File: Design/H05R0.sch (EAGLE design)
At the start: 62 parts, among them J1 1984617_MOD, Q1 ECH8693R-TL-W, Q2 ECH8693R-TL-W, U1 STM32G0B1CEU6QFN_B1CEU6_STM-L, U2 MAX17330X22+, U3 TPS631000DRLR, U4 LD39200PU33R, U5 NCP45521IMNTWG-LDFN8_2X2_ONS, X1 XTALL_CSTCE8M00G52

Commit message: - New version: Schematic finished and reviewed. Other files have not been modified yet for the new design.
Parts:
- removed D2: UCLAMP0501H.TCT, HEXABITZ_RCLS:UCLAMP0501H.TCT
- removed J1: 1984617_MOD, HEXABITZ_CONNECTION_PARTS:1984617_MOD
- removed Q2: ECH8693R-TL-W, HEXABITZ_RCLS:ECH8693R-TL-W
- removed R1: 0.0R, HEXABITZ_RCLS:R-0603
- added BAT_J2: B2P-VH-FB-B_LF__SN_, HEXABITZ_CONNECTION_PARTS:B2P-VH-FB-B_LF__SN_
- added C19: 10uF, HEXABITZ_RCLS:C-0805
- added C20, C6: 1uF, HEXABITZ_RCLS:C-0805
- added C21, C22, C23: 100nF, HEXABITZ_RCLS:C-0603
- added C24: 22nF, HEXABITZ_RCLS:C-0603
- added C7: 4.7uF, HEXABITZ_RCLS:C-0805
- added PIO_J: 3-644456-2, HEXABITZ_USER_INTERFACE_PARTS:3-644456-2
- added R25, R28: 100K, HEXABITZ_RCLS:R-0603
- added R26, R27: 4.7K, HEXABITZ_RCLS:R-0603
- added R29: 100R, HEXABITZ_RCLS:R-0603
- added R30: 0R, HEXABITZ_RCLS:R-0603
- added SJ1, SJ2: (no value), jumper:SJ
- added U6: LDK130C33R, HEXABITZ_ICs:LDK130C33R
- added VBUS_OUT_J: 1984617, HEXABITZ_CONNECTION_PARTS:1984617
- Q1: value ECH8693R-TL-W -> SISF06DN-T1-GE3; device HEXABITZ_RCLS:ECH8693R-TL-W -> HEXABITZ_ICs:SISF06DN-T1-GE3
- R4: value 10 mR -> 5 mR
- R5: value 100K -> 33K
- R6: value 665K -> 220K
- U5: value NCP45521IMNTWG-LDFN8_2X2_ONS -> NCP45521IMNTWG-L
- USB_C: value UJC-HP-G-SMT-TR -> 12401610E4#2A; device HEXABITZ_CONNECTION_PARTS:UJC-HP-G-SMT-TR -> HEXABITZ_CONNECTION_PARTS:12401610E4#2A
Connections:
- net DIS renamed N$24
- removed net CHG: R9.2, U2.CHG
- removed net CSP: C18.1, Q1.SOURCE1, Q2.SOURCE1, R4.2, U2.CSP
- removed net N$13 (its old number): R20.2, R7.2, U3.MODE
- removed net N$4: Q2.DRAIN_1, Q2.DRAIN_2, Q2.DRAIN_3, Q2.DRAIN_4
- removed net N$9: Q1.DRAIN_1, Q1.DRAIN_2, Q1.DRAIN_3, Q1.DRAIN_4
- removed net VSSA: BAT_J.2, C10.1, C11.1, C13.2, C14.2, C17.1, C2.2, C3.-, C4.2, C5.-, C8.-, C9.1, D2.A, EXT_TH_J.1, J1.2, R1.1, R13.1, R14.1, R19.2, R5.1, R7.1, U1.VSS/VSSA, U2.GND, U3.GND, U4.EPAD, USB_C.GND, USB_C.SHIELD
- new net 3V3_OUT: C15.2, SJ2.1, U$1.VDD1, U$1.VDD10, U$1.VDD2, U$1.VDD3, U$1.VDD4, U$1.VDD5, U$1.VDD6, U$1.VDD7, U$1.VDD8, U$1.VDD9, U4.ADJ/SENSE, U4.OUT
- new net 3V3_OUT_EN: R28.2, U4.EN
- new net MCU_3V3: C21.2, C7.1, R11.2, R21.2, R22.2, SJ2.2, U5.VCC, U6.OUT
- new net N$16: R8.2, U3.EN
- new net N$22: R25.1, U6.EN
- new net N$23: R29.2, U5.BLEED
- new net N$25: Q1.G1, R9.1
- new net N$29: C23.2, U5.SR
- new net N$30: C18.1, Q1.S1, R4.2, U2.CSP
- new net N$32: C18.2, R9.2, U2.CHG
- new net VBUS_OUT: C20.1, R29.1, SJ1.2, U5.VOUT, VBUS_OUT_J.1
- new net VBUS_OUT_EN: U5.EN
- new net VBUS_SENSE: C22.1, R26.1, R27.2
- net +3.8V: now also C6.1, R25.2, U6.IN; no longer U4.EN
- net GND: now also BAT_J.2, BAT_J2.2, C10.1, C11.1, C13.2, C14.2, C17.1, C19.2, C2.2, C20.2, C21.1, C22.2, C23.1, C24.1, C3.-, C4.2, C5.-, C6.2, C7.2, C8.-, C9.1, EXT_TH_J.2, PIO_J.2, R13.1, R14.1, R19.2, R27.1, R28.1, R5.1, R7.1, U1.VSS/VSSA, U2.GND, U3.GND, U5.GND, U6.GND, USB_C.GND, USB_C.MH, VBUS_OUT_J.2; no longer R1.2
- net MCU_INT: now also PIO_J.1
- net MCU_SCL: no longer R21.1
- net MCU_SDA: now also R21.1
- net N$10: now also Q1.G2, R10.1; no longer C18.2, Q1.GATE1, Q2.GATE1, R9.1
- net N$15: now also Q1.D1, Q1.D2; no longer Q1.GATE2, Q2.GATE2, R10.1
- net N$18: now also EXT_TH_J.1, R30.1; no longer EXT_TH_J.2
- net N$28: now also R20.1, R7.2, U3.MODE; no longer R8.1, U3.EN
- net VBAT: now also BAT_J2.1, C24.2, R30.2
- net VBUS: now also C19.1, Q1.S2, R20.2, R26.2, R8.1, SJ1.1, U5.VIN; no longer D2.K, J1.1, Q1.SOURCE2, Q2.SOURCE2, R20.1, R8.2
- net VDD: no longer C15.2, R11.2, R21.2, R22.2, U$1.VDD1, U$1.VDD10, U$1.VDD2, U$1.VDD3, U$1.VDD4, U$1.VDD5, U$1.VDD6, U$1.VDD7, U$1.VDD8, U$1.VDD9, U4.ADJ/SENSE, U4.OUT
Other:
- note added: "3"
- note added: "3.3V Out LDO"
- note added: "Active High"
- note added: "Active Low"
- note added: "Charger input"
- note added: "MCU LDO"
- note added: "VBUS Output Switch"
- note removed: "BAT_I2C"
- note removed: "LDO Regulator"
- note removed: "Power input"

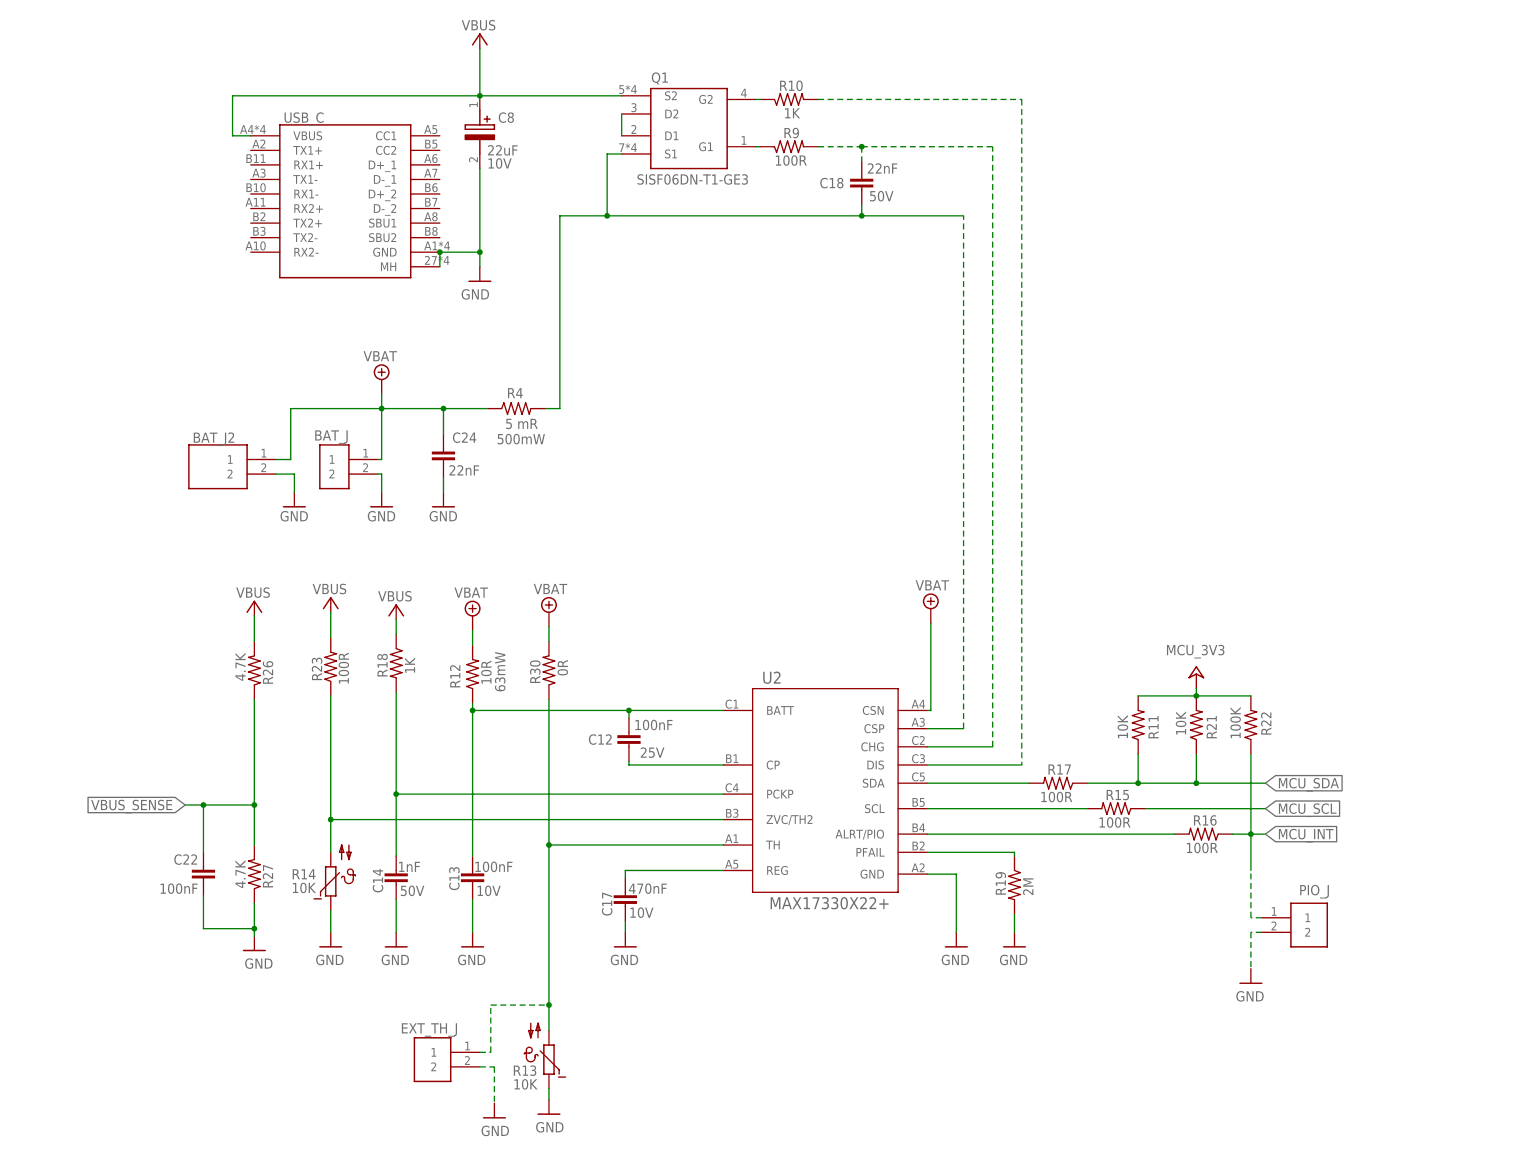
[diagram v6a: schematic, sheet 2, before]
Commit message: -New Version (1b), reviewed and finished - adding the charging detection & current measurement circuit
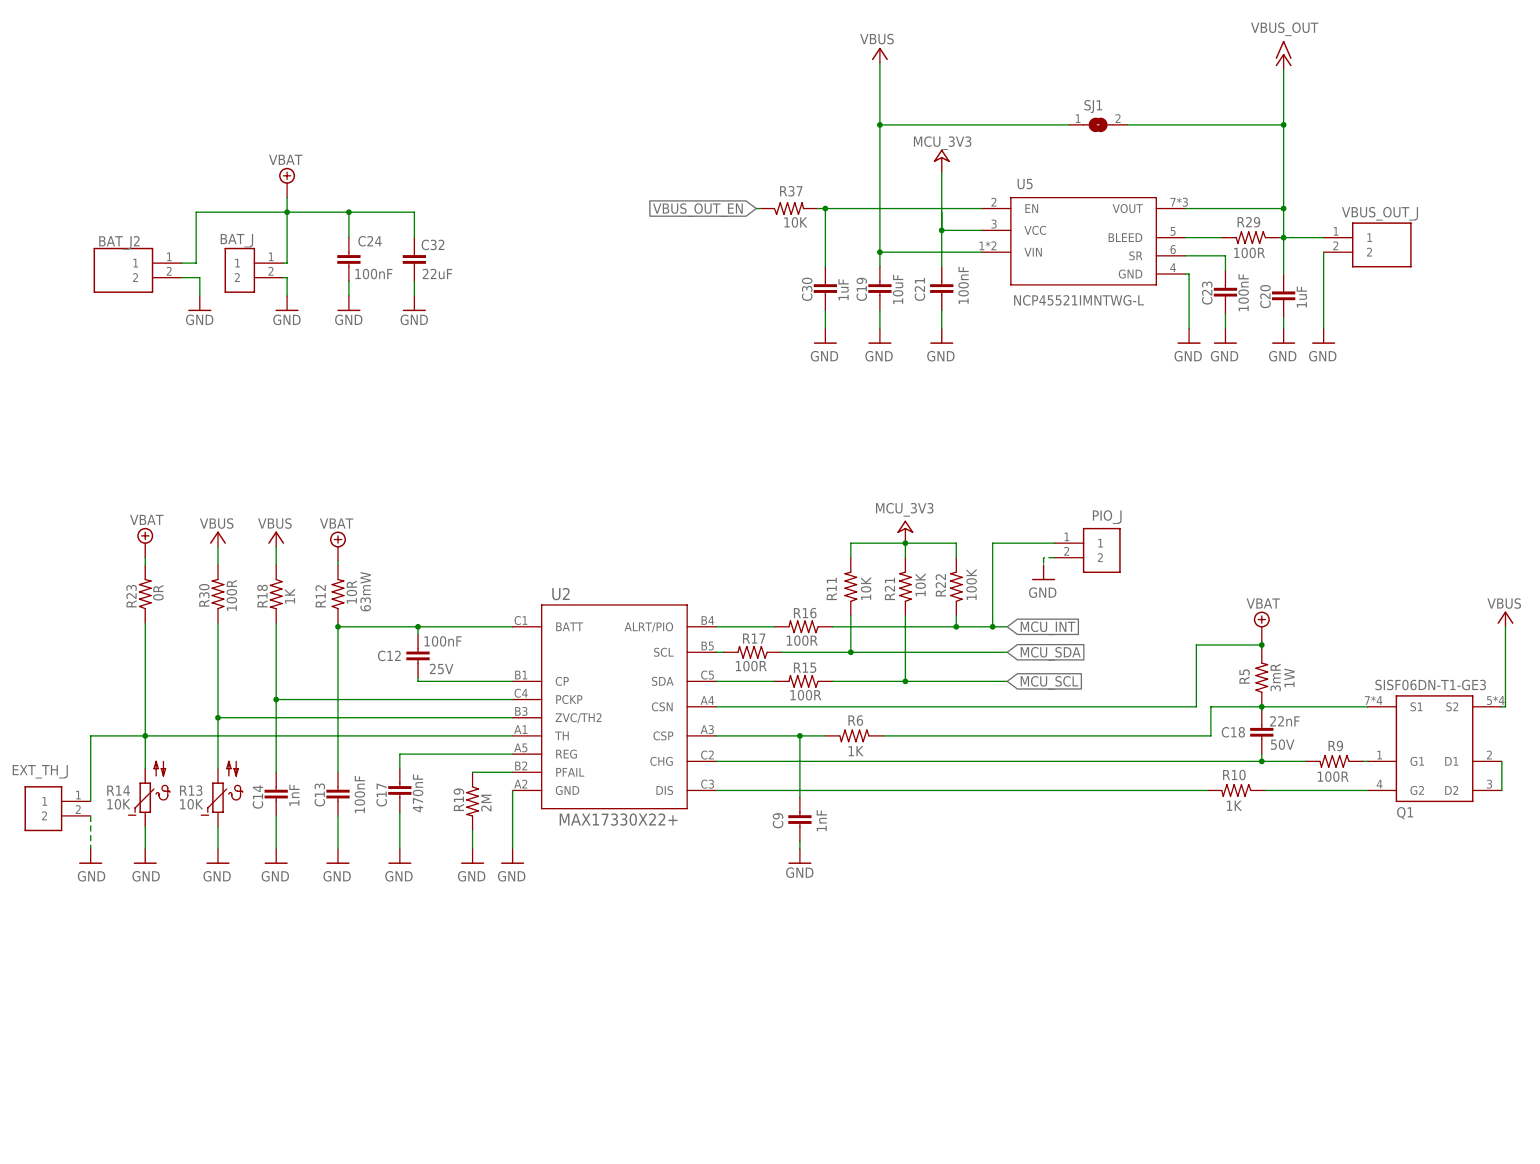
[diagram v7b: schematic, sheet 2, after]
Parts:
- removed L1: DFE252012P-1R0M=P2, HEXABITZ_RCLS:DFE252012P-1R0M=P2
- removed USB_C: 12401610E4#2A, HEXABITZ_CONNECTION_PARTS:12401610E4#2A
- added C25, C26, C27, C31: 100nF, HEXABITZ_RCLS:C-0603
- added C28, C29, C30: 1uF, HEXABITZ_RCLS:C-0805
- added C32: 22uF, HEXABITZ_RCLS:C-0805
- added D2: TL431QDBZR,215, HEXABITZ_RCLS:TL431QDBZR,215
- added D5, D6, D7: CUS10S30,H3F, HEXABITZ_RCLS:CUS10S30,H3F
- added J1: 12401610E4#2A12401610E42A, HEXABITZ_CONNECTION_PARTS:12401610E4#2A12401610E42A
- added R1: 10 mR, HEXABITZ_RCLS:R-0805
- added R31: 20K, HEXABITZ_RCLS:R-0603
- added R32: 27K, HEXABITZ_RCLS:R-0603
- added R33: 2K, HEXABITZ_RCLS:R-0603
- added R34: 100K, HEXABITZ_RCLS:R-0603
- added R35, R36: 22K, HEXABITZ_RCLS:R-0603
- added R37, R39: 10K, HEXABITZ_RCLS:R-0603
- added R38: 1M, HEXABITZ_RCLS:R-0603
- added SJ3: (no value), HEXABITZ_USER_INTERFACE_PARTS:SJ
- C10: value 47uF -> 33nF; MPN CL10A476MQ8QRN -> (none); VOLTAGE_RATING 6.3V -> 50V
- C11, C15: device HEXABITZ_RCLS:C-0603 -> HEXABITZ_RCLS:C-0805
- C16: value 22pF -> 33nF; STATE DNP -> (none); VOLTAGE_RATING (none) -> 50V
- C24: value 22nF -> 100nF
- C8: device HEXABITZ_RCLS:T491B226K010AT -> HEXABITZ_RCLS:C-0805; VOLTAGE 10V -> (none)
- C9: value 22uF -> 1nF; MPN GRM187R61A226ME15 -> (none); VOLTAGE_RATING 10V -> 50V
- R20: value 100K -> 49.9K
- R23: RESISTANCE 100R -> 0R
- R25, R28: value 100K -> 220K
- R26: value 4.7K -> 47K
- R27: value 4.7K -> 20K
- R30: value 0R -> 100R
- R4: value 5 mR -> 1K; device HEXABITZ_RCLS:R-0805 -> HEXABITZ_RCLS:R-0603; POWR 500mW -> (none); STATE (none) -> DNP
- R5: value 33K -> 3mR; device HEXABITZ_RCLS:R-0603 -> HEXABITZ_RCLS:R_1206R1206; MPN (none) -> WFC12063L000FE66; OCTOPART_URL (none) -> https://www.digikey.com/en/products/detail/vishay-dale/WFC1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; POWER (none) -> 1W; TOLERANCE 1% -> (none)
- R6: value 220K -> 1K; TOLERANCE 1% -> (none)
- R7: value 100K -> 1K; STATE (none) -> DNP
- R8: value 100K -> 49.9K; STATE (none) -> DNP
- SJ1, SJ2: device jumper:SJ -> HEXABITZ_USER_INTERFACE_PARTS:SJ
- U3: value TPS631000DRLR -> TSV772IQ2T; device HEXABITZ_ICs:TPS631000DRLRTPS631000DRLR_TEX -> HEXABITZ_ICs:TSV772IQ2T
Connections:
- net BAT_ALRT renamed N$15
- net N$2 renamed IND_LED
- removed net +3.8V: C10.2, C11.2, C16.1, C6.1, R25.2, R6.1, U3.VOUT, U4.IN, U6.IN
- removed net BAT_SCL: R15.2, U2.SCL
- removed net BAT_SDA: R17.2, U2.SDA
- removed net N$13 (its old number): L1.1, U3.LX1
- removed net N$18 (its old number): EXT_TH_J.1, R13.2, R30.1, U2.TH
- removed net USART5_RX: U$1.SD1, U1.PD2
- removed net USART5_TX: U$1.SU1, U1.PD3
- removed net VDD: D4.C, FB1.2
- new net 3V3_OUT_PG: R39.1, U1.PB13, U4.PG
- new net CHARGER_CURRENT_SENSE: C10.2, R20.2, U1.PB0, U3.OUT1
- new net CHARGER_DETECT: D5.A, R38.2, U3.OUT2
- new net MCU_LDO_EN: D6.A, U1.PB2
- new net N$11: C9.2, R6.2, U2.CSP
- new net N$12: C18.1, Q1.S1, R5.1, R6.1
- new net N$24: R15.2, U2.SDA
- new net N$32: D5.K, D6.K, D7.K, R35.1
- new net N$35: D7.A, SJ3.1
- new net N$4: C30.2, R37.2, U5.EN
- new net USART4_RX: U$1.SD1, U1.PA1
- new net USART4_TX: U$1.SU1, U1.PA0
- new net VBUS1: C26.2, R31.1, R32.2, R38.1, U3.IN2+
- new net VBUS2: C27.2, D2.1, D2.2, R33.1, R34.2, U3.IN2-
- new net VCHARGER: C25.2, C31.2, C8.1, J1.VBUS, R1.1, R7.2, U3.VCC+
- new net VREF: C4.1, C5.+, U1.VREF+
- net 3V3_OUT: now also U4.SENSE; no longer U4.ADJ/SENSE
- net 3V3_OUT_EN: now also R36.1, U1.PB12; no longer R28.2, U4.EN
- net GND: now also C16.1, C25.1, C26.1, C27.1, C28.1, C29.1, C30.1, C31.1, C32.2, C8.2, D2.3, J1.GND, J1.MH, R25.2, R32.1, R34.1, R8.1, U3.VCC-; no longer C10.1, C8.-, R5.1, R7.1, U1.PB12, U1.PB13, U3.GND, USB_C.GND, USB_C.MH
- net MCU_3V3: now also D4.C, FB1.2, R39.2
- net MCU_INT: now also U1.PA5; no longer U1.PB0
- net MCU_SCL: now also R21.1
- net MCU_SDA: no longer R21.1
- net N$14: now also C10.1, R20.1, R4.1, U3.IN1-; no longer L1.2, U3.LX2
- net N$16: now also R17.2, U2.SCL; no longer R8.2, U3.EN
- net N$17: now also R13.2, R30.1; no longer R14.2, R23.1
- net N$22: now also C28.2, R35.2
- net N$27: now also R7.1, R8.2, U3.IN1+; no longer R5.2, R6.2, U3.FB
- net N$28: now also EXT_TH_J.1, R14.2, R23.1, U2.TH; no longer R20.1, R7.2, U3.MODE
- net N$30: now also C29.2, R28.2, R36.2, U4.EN; no longer C18.1, Q1.S1, R4.2, U2.CSP
- net STATUS_LED: now also U1.PA8; no longer U1.PB4
- net USART1_RX: now also U$1.SD4; no longer U$1.SD5
- net USART1_TX: now also U$1.SU4; no longer U$1.SU5
- net USART3_RX: now also U$1.SD3; no longer U$1.SD4
- net USART3_TX: now also U$1.SU3; no longer U$1.SU4
- net USART6_RX: now also U$1.SD5, U1.PB9; no longer U$1.SD3, U1.PA5
- net USART6_TX: now also U$1.SU5, U1.PB8; no longer U$1.SU3, U1.PA4
- net VBAT: now also C32.1, R23.2, R5.2; no longer R30.2, R4.1
- net VBUS: now also C11.2, C6.1, R1.2, R30.2, R31.2, R33.2, R4.2, SJ3.2, U4.IN, U6.IN; no longer C8.+, C9.2, R20.2, R23.2, R8.1, U3.VIN, USB_C.VBUS
- net VBUS_OUT_EN: now also R37.1, U1.PA4; no longer U5.EN
- net VBUS_SENSE: now also U1.PB1
- net VDDA: no longer C4.1, C5.+, U1.VBAT, U1.VREF+
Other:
- note added: "3.3V_OUT LDO"
- note added: "Charger detection & Current measurement"
- note added: "Gain = 50 0.5V @ 1A 2.5V @ 5A"
- note added: "MAX OUTPUT CURRENT = 1 A"
- note added: "MAX OUTPUT CURRENT = 10A"
- note added: "VOUT<0.8*3.3V ....... PG=LOW"
- note added: "VOUT>0.92*3.3V ....... PG=HIGH"
- note added: "V_Charger Range = (4.5 - 5.5 ) Volt"
- note added: "Vth-High = 4.43V Vth-Low = 4.34V"
- note removed: "3.3V Out LDO"
- note removed: "Buck-Boost Converter"
- note removed: "MAX OUTPUT CURRENT = 2 A"
- note removed: "VBUS RANGE = (1.65 - 5.5 ) Volt"
- moved on the sheet: BAT_J, BAT_J2, C1, C10, C11, C12, C13, C14, C15, C16, C17, C18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
